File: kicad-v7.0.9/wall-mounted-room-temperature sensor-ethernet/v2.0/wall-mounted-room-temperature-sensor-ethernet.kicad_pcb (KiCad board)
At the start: 2 copper layers, 107 x 90 mm, 165 parts, among them J1 rj45, P1 2x3_MLW06A, P2 1x9_pin_socket, Q1 DMG2307L, Q2 FDC2512, SW1 TVAF18BB, SW2 TVAF18BB, SW3 B3F-4150, SW4 B3F-4150, SW5 B3F-4150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

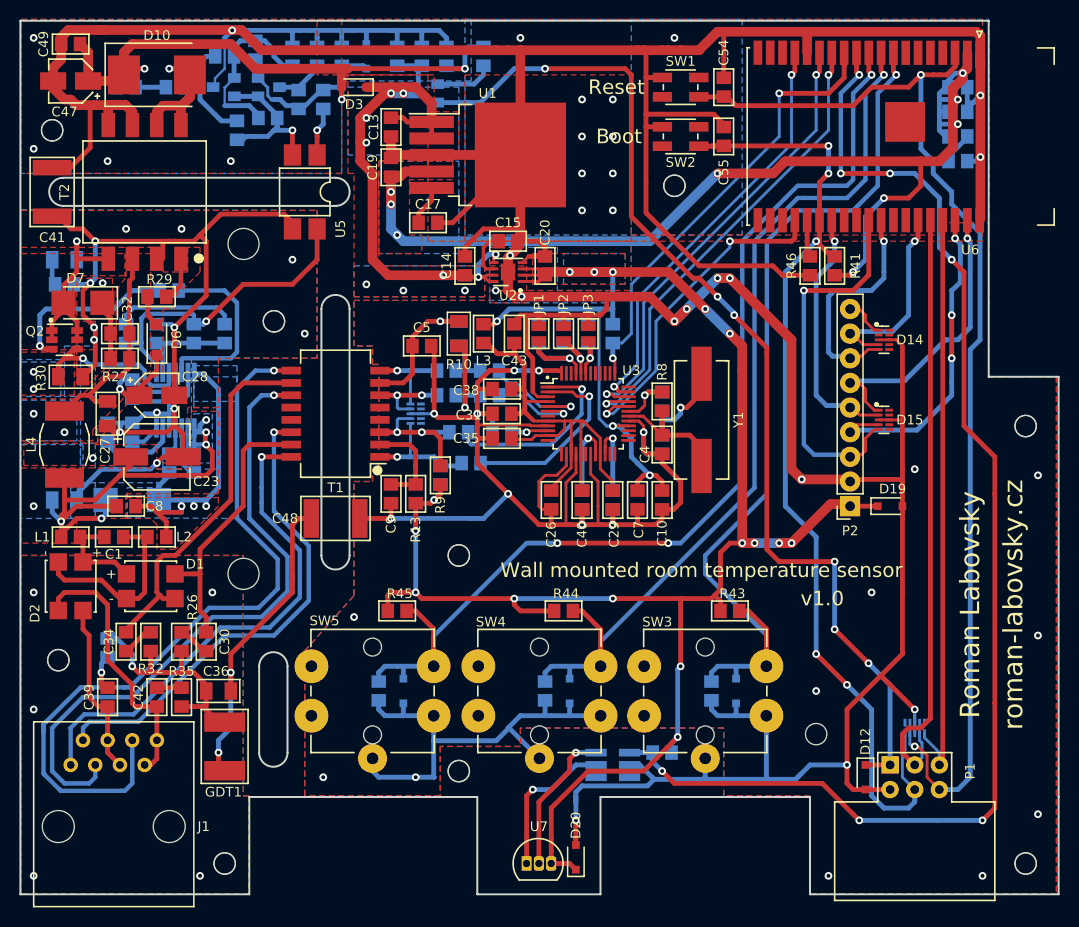
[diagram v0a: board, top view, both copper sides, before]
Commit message: Wall mounted room temperature sensor - ethernet. Change library. Small changes in schematic a PCB.
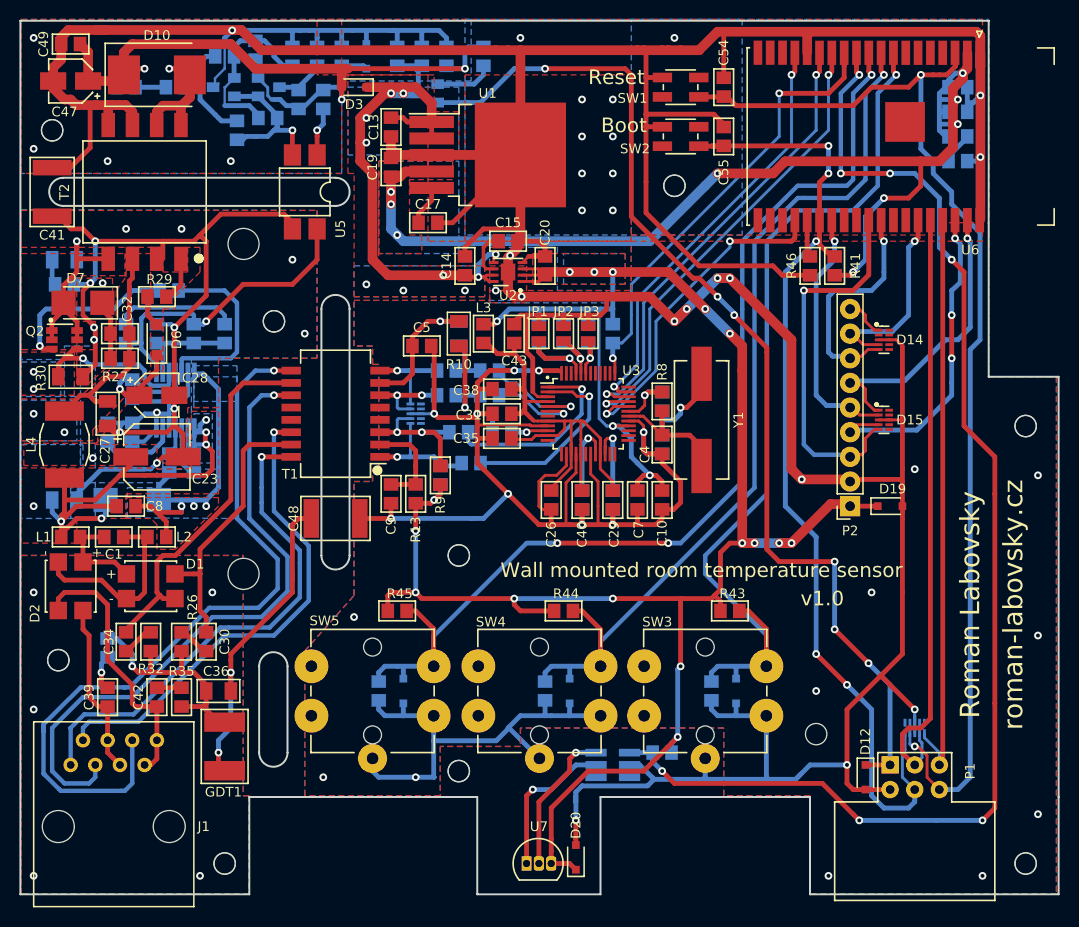
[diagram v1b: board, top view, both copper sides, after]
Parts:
- removed ~ (x10): mounting_hole_2.2mm_4.4mm, mounting_hole_rl:mounting_hole_2.2mm_4.4mm
- removed ~ (x2): mounting_hole_3.2mm_5.5mm, mounting_hole_rl:mounting_hole_3.2mm_5.5mm
- added H1: mounting_hole_2.2x4.4mm, mounting_hole_rl:mounting_hole_2.2x4.4mm, F.Cu at (41.3, 80.0)
- added H10: mounting_hole_2.2x4.4mm, mounting_hole_rl:mounting_hole_2.2x4.4mm, F.Cu at (141.6, 155.6)
- added H11: mounting_hole_3.2x5.5mm, mounting_hole_rl:mounting_hole_3.2x5.5mm, F.Cu at (61.0, 91.7)
- added H12: mounting_hole_3.2x5.5mm, mounting_hole_rl:mounting_hole_3.2x5.5mm, F.Cu at (61.0, 125.7)
- added H2: mounting_hole_2.2x4.4mm, mounting_hole_rl:mounting_hole_2.2x4.4mm, F.Cu at (105.4, 85.7)
- added H3: mounting_hole_2.2x4.4mm, mounting_hole_rl:mounting_hole_2.2x4.4mm, F.Cu at (64.1, 99.7)
- added H4: mounting_hole_2.2x4.4mm, mounting_hole_rl:mounting_hole_2.2x4.4mm, F.Cu at (141.6, 110.5)
- added H5: mounting_hole_2.2x4.4mm, mounting_hole_rl:mounting_hole_2.2x4.4mm, F.Cu at (83.2, 123.8)
- added H6: mounting_hole_2.2x4.4mm, mounting_hole_rl:mounting_hole_2.2x4.4mm, F.Cu at (41.9, 134.6)
- added H7: mounting_hole_2.2x4.4mm, mounting_hole_rl:mounting_hole_2.2x4.4mm, F.Cu at (83.2, 146.1)
- added H8: mounting_hole_2.2x4.4mm, mounting_hole_rl:mounting_hole_2.2x4.4mm, F.Cu at (120.0, 142.2)
- added H9: mounting_hole_2.2x4.4mm, mounting_hole_rl:mounting_hole_2.2x4.4mm, F.Cu at (59.1, 155.6)
- C23: footprint elec_capacitor_smd_rl:elec_c_6.3x7.7 -> capacitor_elec_smd_rl:c_elec_6.3x7.7
- C28, C47: footprint elec_capacitor_smd_rl:elec_c_4x5.8 -> capacitor_elec_smd_rl:c_elec_4x5.8
- C41, C48: footprint capacitor_smd_rl:c_1812_gal_space -> capacitor_smd_rl:c_1812
- J1: value rj45 -> 54601-908WPLF
- JP1, JP2, JP3: value solder_jumper_2_open -> solder_jumper_2_open_rect_1x1.5mm; footprint solder_jumper_rl:solder_jumper_2_open_rect_1x1,5mm -> solder_jumper_rl:solder_jumper_2_open_rect_1x1.5mm
- L1, L2, L3: footprint resistor_smd_rl:r_0805 -> inductor_smd_rl:ferrite_bead_0805
- L4: value 4,7uH/1,5A -> DO1608C-472ML
- P2: value 1x9_pin_socket -> DS1023-1-9S21
